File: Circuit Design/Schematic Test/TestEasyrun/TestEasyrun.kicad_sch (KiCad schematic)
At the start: 26 parts, among them U1 ESP32-WROOM-32

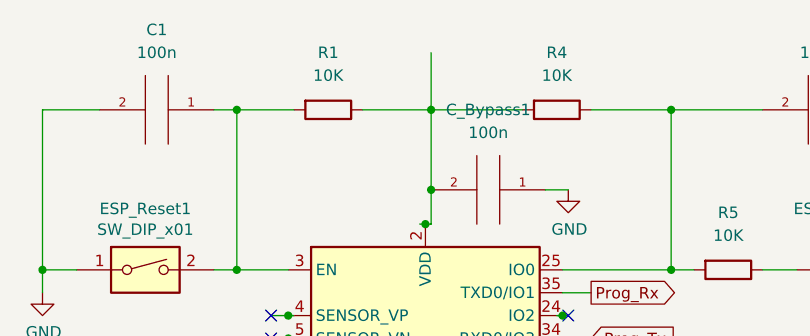
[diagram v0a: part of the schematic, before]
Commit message: Huellas sin botones ni potencia
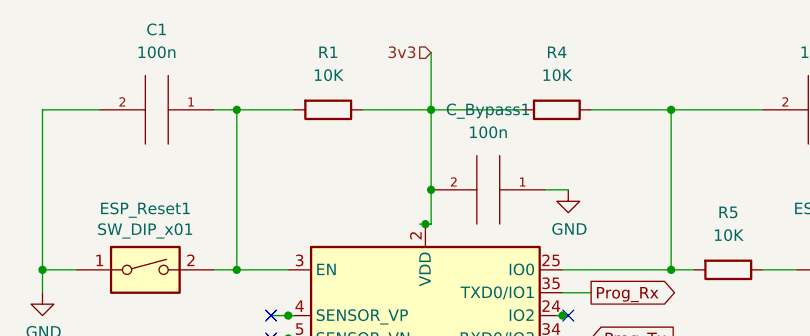
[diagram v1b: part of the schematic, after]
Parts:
- Display1: footprint Connector_PinSocket_2.54mm:PinSocket_1x04_P2.54mm_Vertical -> (none)
- J_Lector_1, J_Lector_2, J_Lector_3: footprint (none) -> Connector_PinHeader_2.54mm:PinHeader_1x08_P2.54mm_Vertical
- J_Motor_1, J_Motor_2: footprint (none) -> Connector_PinHeader_2.54mm:PinHeader_1x03_P2.54mm_Vertical
- R_prog1: value 39 -> (none)
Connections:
- net 3v3: now also C_Bypass1.2, R1.1, R4.2, U1.2 (VDD)
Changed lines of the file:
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@@
+    (effects (font (size 1.27 1.27)) (justify right))
+  )
+  (hierarchical_label "3v3" (shape input) (at 134.62 19.05 180)
     (effects (font (size 1.27 1.27)) (justify right))
   )
@@
       (effects (font (size 1.27 1.27)) (justify left))
     )
-    (property "Footprint" "" (id 2) (at 204.47 144.78 0)
+    (property "Footprint" "Connector_PinHeader_2.54mm:PinHeader_1x08_P2.54mm_Vertical" (id 2) (at 204.47 144.78 0)
       (effects (font (size 1.27 1.27)) hide)
     )
@@
       (effects (font (size 1.27 1.27)) (justify left))
     )
-    (property "Footprint" "" (id 2) (at 254 110.49 0)
+    (property "Footprint" "Connector_PinHeader_2.54mm:PinHeader_1x03_P2.54mm_Vertical" (id 2) (at 254 110.49 0)
       (effects (font (size 1.27 1.27)) hide)
     )
@@
     (property "Reference" "Display1" (id 0) (at 32.385 115.57 0))
     (property "Value" "Conn_01x04_Female" (id 1) (at 32.385 118.11 0))
-    (property "Footprint" "Connector_PinSocket_2.54mm:PinSocket_1x04_P2.54mm_Vertical" (id 2) (at 31.75 123.19 0)
+    (property "Footprint" "" (id 2) (at 31.75 123.19 0)
       (effects (font (size 1.27 1.27)) hide)
     )
@@
       (effects (font (size 1.27 1.27)) (justify left))
     )
-    (property "Footprint" "" (id 2) (at 254 91.44 0)
+    (property "Footprint" "Connector_PinHeader_2.54mm:PinHeader_1x03_P2.54mm_Vertical" (id 2) (at 254 91.44 0)
       (effects (font (size 1.27 1.27)) hide)
     )
@@
     (in_bom yes) (on_board yes)
     (property "Reference" "R_prog1" (id 0) (at 247.015 129.54 90))
-    (property "Value" "39" (id 1) (at 246.38 126.5936 90)
-      (effects (font (size 1.27 1.27)) hide)
-    )
+    (property "Value" "" (id 1) (at 246.38 126.5936 90))
     (property "Footprint" "" (id 2) (at 246.38 127.762 90)
       (effects (font (size 1.27 1.27)) hide)
@@
       (effects (font (size 1.27 1.27)) (justify left))
     )
-    (property "Footprint" "" (id 2) (at 204.47 119.38 0)
+    (property "Footprint" "Connector_PinHeader_2.54mm:PinHeader_1x08_P2.54mm_Vertical" (id 2) (at 204.47 119.38 0)
       (effects (font (size 1.27 1.27)) hide)
     )
@@
       (effects (font (size 1.27 1.27)) (justify left))
     )
-    (property "Footprint" "" (id 2) (at 204.47 92.71 0)
+    (property "Footprint" "Connector_PinHeader_2.54mm:PinHeader_1x08_P2.54mm_Vertical" (id 2) (at 204.47 92.71 0)
       (effects (font (size 1.27 1.27)) hide)
     )
@@
     )
     (path "/b7cc3d0e-1fc8-4cd7-a3c2-1509da6ebf42"
-      (reference "C1") (unit 1) (value "100n") (footprint "")
+      (reference "C1") (unit 1) (value "100n") (footprint "Capacitor_SMD:C_0805_2012Metric_Pad1.18x1.45mm_HandSolder")
     )
     (path "/99a27256-a88a-4355-b453-612ad2615aaf"
-      (reference "C2") (unit 1) (value "100n") (footprint "")
+      (reference "C2") (unit 1) (value "100n") (footprint "Capacitor_SMD:C_0805_2012Metric_Pad1.18x1.45mm_HandSolder")
     )
     (path "/1347a48f-a9f7-470c-893f-af03f52f8d81"
-      (reference "C_Bypass1") (unit 1) (value "100n") (footprint "")
+      (reference "C_Bypass1") (unit 1) (value "100n") (footprint "Capacitor_SMD:C_0805_2012Metric_Pad1.18x1.45mm_HandSolder")
     )
     (path "/b212d6ec-c50e-4013-a932-130ab8b4a4f5"
@@
     )
     (path "/47f1e5ed-3a1b-4dbd-971b-d6b2b4751745"
-      (reference "Conn_Prog1") (unit 1) (value "Conn_01x06_Male") (footprint "")
+      (reference "Conn_Prog1") (unit 1) (value "Conn_01x06_Male") (footprint "Connector_PinSocket_2.54mm:PinSocket_1x06_P2.54mm_Vertical")
     )
     (path "/5eb1f7ee-9a6a-4ec6-9280-6b1b89d7fdfb"
@@
     )
     (path "/05f67689-b87d-4a73-ba19-8cfc59729f07"
-      (reference "ESP_Prog_Enable1") (unit 1) (value "SW_DIP_x02") (footprint "")
+      (reference "ESP_Prog_Enable1") (unit 1) (value "SW_DIP_x02") (footprint "Button_Switch_SMD:SW_SPST_CK_RS282G05A3")
     )
     (path "/b69519ee-5035-4725-9f32-90c7cfdb2f78"
-      (reference "ESP_Reset1") (unit 1) (value "SW_DIP_x01") (footprint "")
+      (reference "ESP_Reset1") (unit 1) (value "SW_DIP_x01") (footprint "Button_Switch_SMD:SW_SPST_CK_RS282G05A3")
     )
     (path "/8c4bbe2b-6fb3-4548-8dd3-0f1711d4f6b1"
-      (reference "J_I2C1") (unit 1) (value "Conn_01x05_Male") (footprint "")
+      (reference "J_I2C1") (unit 1) (value "Conn_01x05_Male") (footprint "Connector_PinHeader_2.54mm:PinHeader_1x05_P2.54mm_Vertical")
     )
     (path "/b710020c-0f3a-4776-a938-eddc58b26b95"
@@
     )
     (path "/250658cf-3442-4875-98b9-880ff77de779"
-      (reference "LED_prog1") (unit 1) (value "LED") (footprint "")
+      (reference "LED_prog1") (unit 1) (value "LED") (footprint "LED_SMD:LED_0805_2012Metric_Pad1.15x1.40mm_HandSolder")
     )
     (path "/711d27c5-efee-45ca-9b31-41d211608a1f"
-      (reference "Pull_Down_Miso_Res1") (unit 1) (value "10k") (footprint "")
+      (reference "Pull_Down_Miso_Res1") (unit 1) (value "10k") (footprint "Resistor_SMD:R_0805_2012Metric_Pad1.20x1.40mm_HandSolder")
     )
     (path "/3a3c2d06-2914-4049-8266-3e33b3477ac7"
-      (reference "R1") (unit 1) (value "10K") (footprint "")
+      (reference "R1") (unit 1) (value "10K") (footprint "Resistor_SMD:R_0805_2012Metric_Pad1.20x1.40mm_HandSolder")
     )
     (path "/1e3639f5-e7e3-4694-9294-3921c4c3d8d8"
-      (reference "R2") (unit 1) (value "10K") (footprint "")
+      (reference "R2") (unit 1) (value "10K") (footprint "Resistor_SMD:R_0805_2012Metric_Pad1.20x1.40mm_HandSolder")
     )
     (path "/bfb424f2-8d7e-4d71-b295-e557e237f849"
-      (reference "R3") (unit 1) (value "10K") (footprint "")
+      (reference "R3") (unit 1) (value "10K") (footprint "Resistor_SMD:R_0805_2012Metric_Pad1.20x1.40mm_HandSolder")
     )
     (path "/0b95d5f8-be59-4aa4-9e3b-2ddb0751a97c"
-      (reference "R4") (unit 1) (value "10K") (footprint "")
+      (reference "R4") (unit 1) (value "10K") (footprint "Resistor_SMD:R_0805_2012Metric_Pad1.20x1.40mm_HandSolder")
     )
     (path "/ee202a96-96ee-464e-a148-4b76788af37e"
-      (reference "R5") (unit 1) (value "10K") (footprint "")
+      (reference "R5") (unit 1) (value "10K") (footprint "Resistor_SMD:R_0805_2012Metric_Pad1.20x1.40mm_HandSolder")
     )
     (path "/6ee20d1c-a46d-41e5-9769-e0e93e111749"
-      (reference "R_prog1") (unit 1) (value "39") (footprint "")
+      (reference "R_prog1") (unit 1) (value "47") (footprint "Resistor_SMD:R_0805_2012Metric_Pad1.20x1.40mm_HandSolder")
     )
     (path "/7a371838-7673-4e2a-955b-9b6e37993916"

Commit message: Power integration
Power integration
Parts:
- removed Conn_Power1: Conn_01x03_Male, symbol Connector:Conn_01x03_Male
- added J_Tap_1, J_Tap_2, J_gnd: 62409-1, TE_62409-1, symbol Connector_Faston:62409-1
- C1, C2, C_Bypass1: footprint (none) -> Capacitor_SMD:C_0805_2012Metric_Pad1.18x1.45mm_HandSolder
- Conn_Prog1: footprint (none) -> Connector_PinSocket_2.54mm:PinSocket_1x06_P2.54mm_Vertical
- Display1: footprint (none) -> Connector_PinSocket_2.54mm:PinSocket_1x04_P2.54mm_Vertical
- ESP_Prog_Enable1, ESP_Reset1: footprint (none) -> Button_Switch_SMD:SW_SPST_CK_RS282G05A3
- J_I2C1: footprint (none) -> Connector_PinHeader_2.54mm:PinHeader_1x05_P2.54mm_Vertical
- LED_prog1: footprint (none) -> LED_SMD:LED_0805_2012Metric_Pad1.15x1.40mm_HandSolder
- Pull_Down_Miso_Res1, R1, R2, R3, R4, R5: footprint (none) -> Resistor_SMD:R_0805_2012Metric_Pad1.20x1.40mm_HandSolder
- R_prog1: value (none) -> 47; footprint (none) -> Resistor_SMD:R_0805_2012Metric_Pad1.20x1.40mm_HandSolder
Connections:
- net PowerModule/R_Gnd: now also J_gnd.1 (P1), J_gnd.2 (P1)
- new net PowerModule/Tab_2: J_Tap_2.1 (P1), J_Tap_2.2 (P1)
- new net PowerModule/Tap_1: J_Tap_1.1 (P1), J_Tap_1.2 (P1)
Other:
- sheet PowerModule ports: added Tab_2, Tap_1; removed N, Ph
